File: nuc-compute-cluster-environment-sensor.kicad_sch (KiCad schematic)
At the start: 114 parts, among them J17 USB-C_GCT_USB4105-GF-A, J18 JST_SH_1x4_SM04B-SRSS-TB-LF-SN, U27 FT4232H_VQFN, U28 AP7370-33SA-7, U29 STM32G474CET6, U30 MB85RC1MTPNF-G, U31 SHT45, U32 BME280, Y2 Resonator_12MHz_ABM3B, Y3 Resonator_32.768kHz_ABS06, Y4 Resonator_8MHz_ABM3B

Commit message: 2nd part of review changes
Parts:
- added C104, C105: C_100n_0402, antmicro-footprints:C_0402_1005Metric, symbol antmicroCapacitors0402:C_100n_0402
- C68: DNP DNP -> (none)
- gave numbers to parts that had none: 2
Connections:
- net FTDI_+1V8: now also C104.1, C105.1
- net GND: now also C104.2, C105.2
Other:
- moved on the sheet: C92, TP60

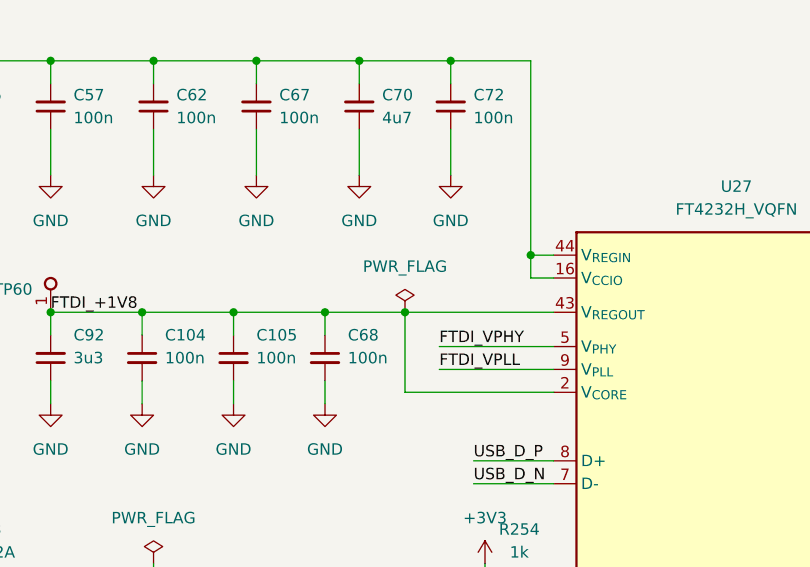
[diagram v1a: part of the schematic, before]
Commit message: Cleaning ERC on schematic
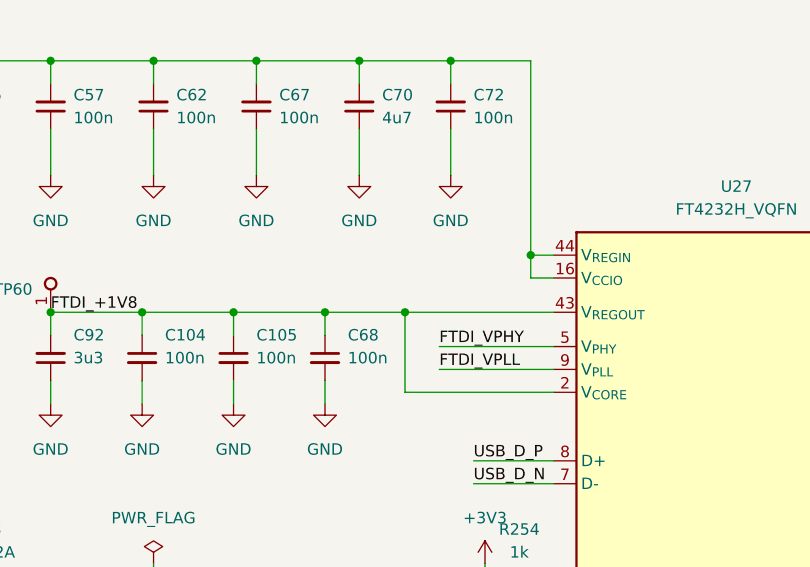
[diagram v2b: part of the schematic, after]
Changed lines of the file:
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@@
     (pin "2")
-  )
-  (symbol (lib_id "antmicropower:PWR_FLAG") (at 76.2 184.15 0) (unit 1)
-    (in_bom yes) (on_board yes) (fields_autoplaced)
-    (property "Reference" "#FLG07" (id 0) (at 76.2 182.245 0)
-      (effects (font (size 1.27 1.27)) hide)
-    )
-    (property "Value" "PWR_FLAG" (id 1) (at 76.2 179.07 0))
-    (property "Footprint" "" (id 2) (at 76.2 184.15 0)
-      (effects (font (size 1.27 1.27)) hide)
-    )
-    (property "Datasheet" "" (id 3) (at 76.2 184.15 0)
-      (effects (font (size 1.27 1.27)) hide)
-    )
-    (pin "1")
   )
   (symbol (lib_name "R_100k_0402_4") (lib_id "antmicroResistors0402:R_100k_0402") (at 307.34 139.7 90) (unit 1)

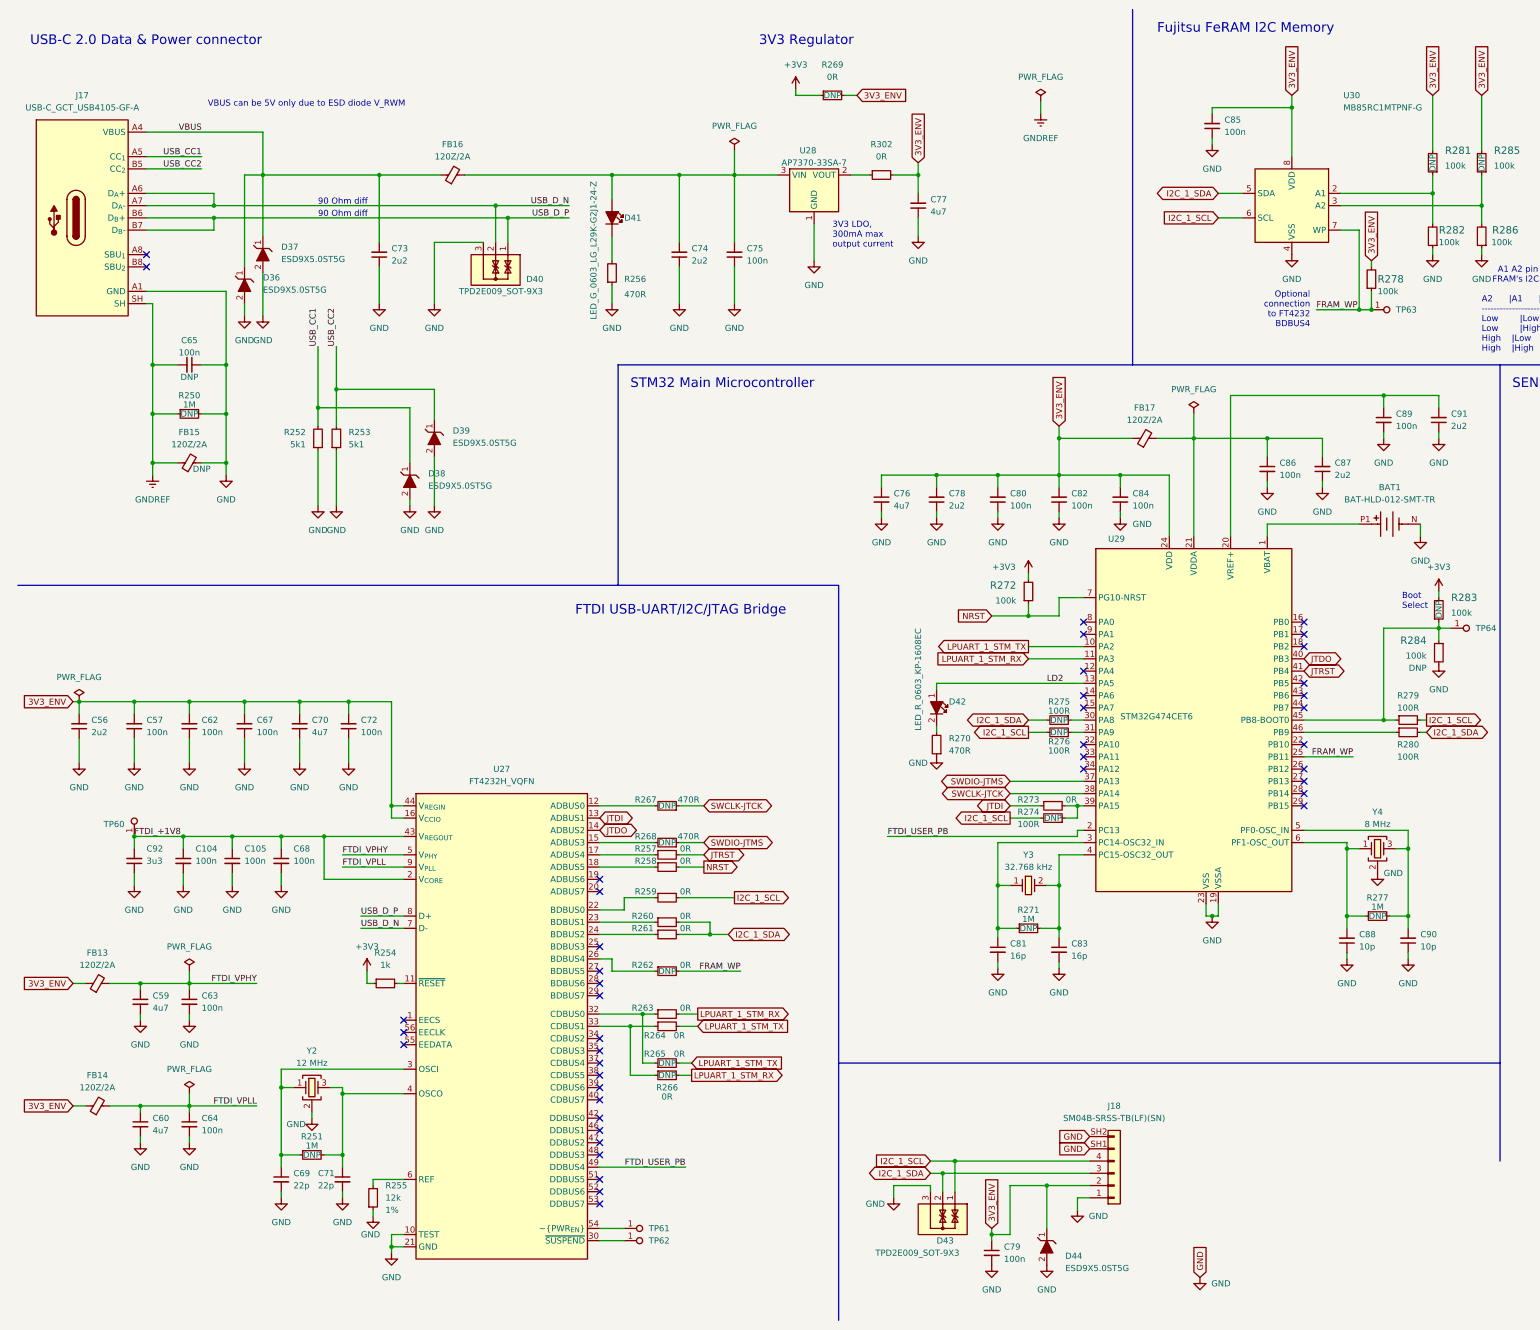
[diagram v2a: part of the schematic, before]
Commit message: Fix possible ERC errors
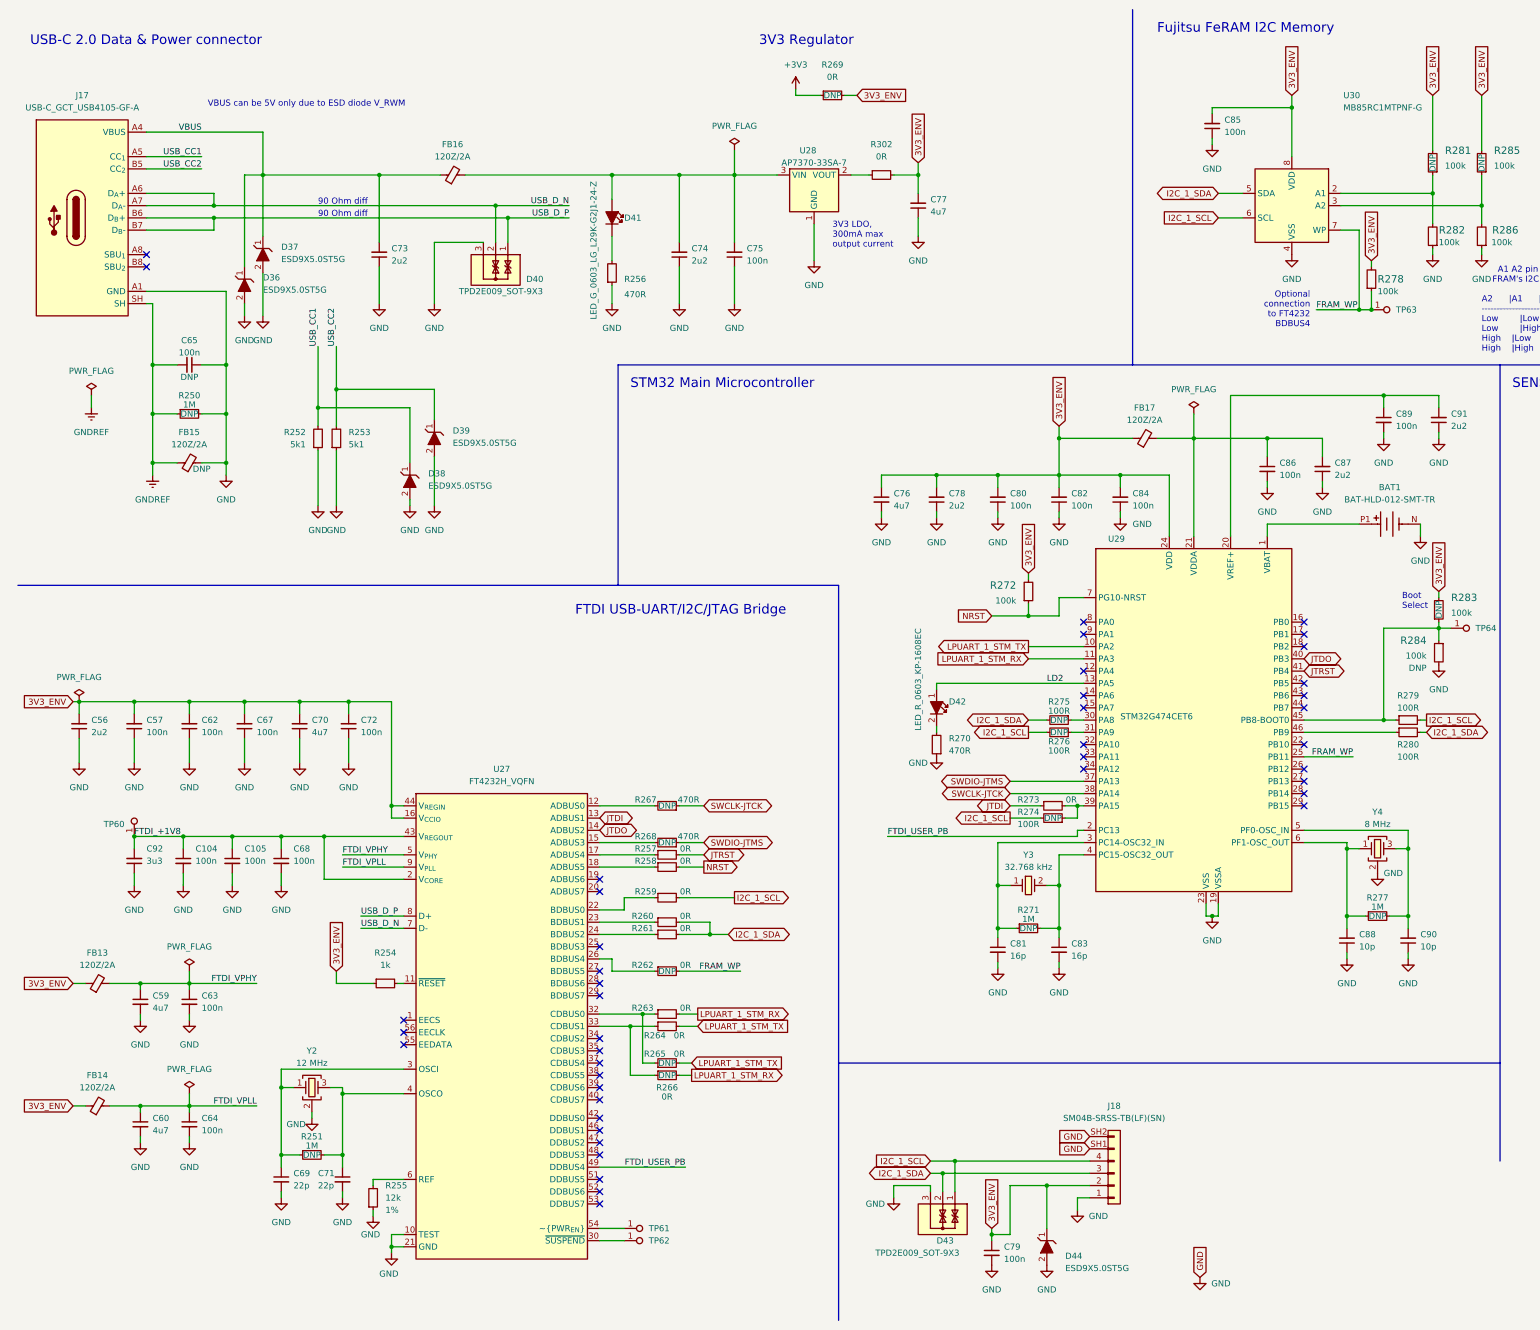
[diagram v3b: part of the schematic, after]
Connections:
- net +3V3: no longer R254.1, R272.2, R283.2
- net 3V3_ENV: now also R254.1, R272.2, R283.2

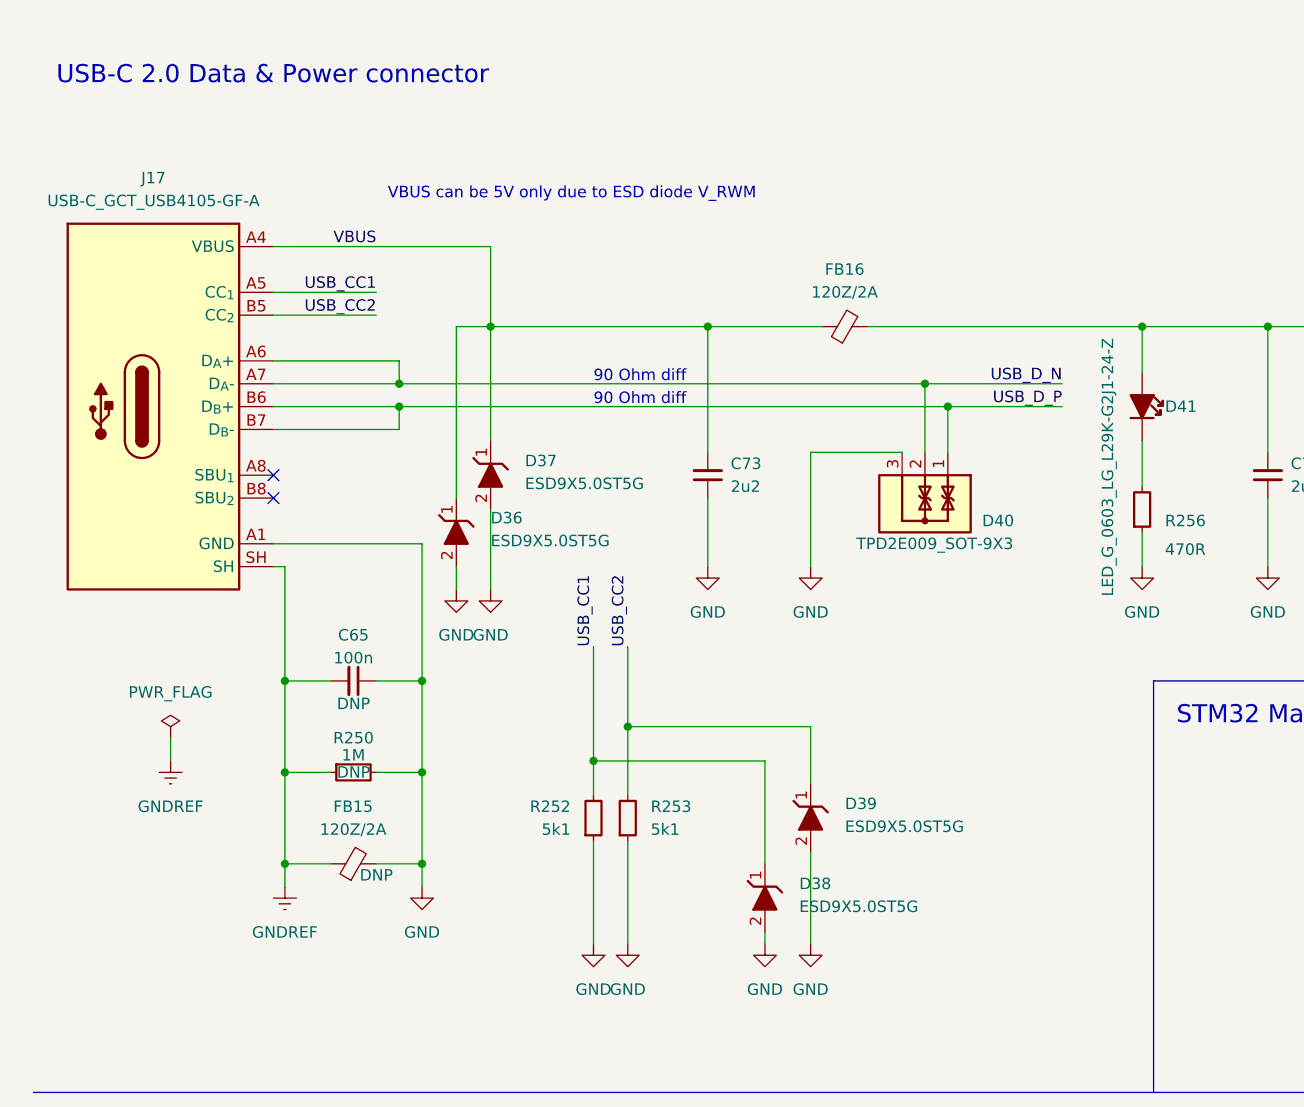
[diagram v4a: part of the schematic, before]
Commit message: Route fan signals for channel 1 and 2
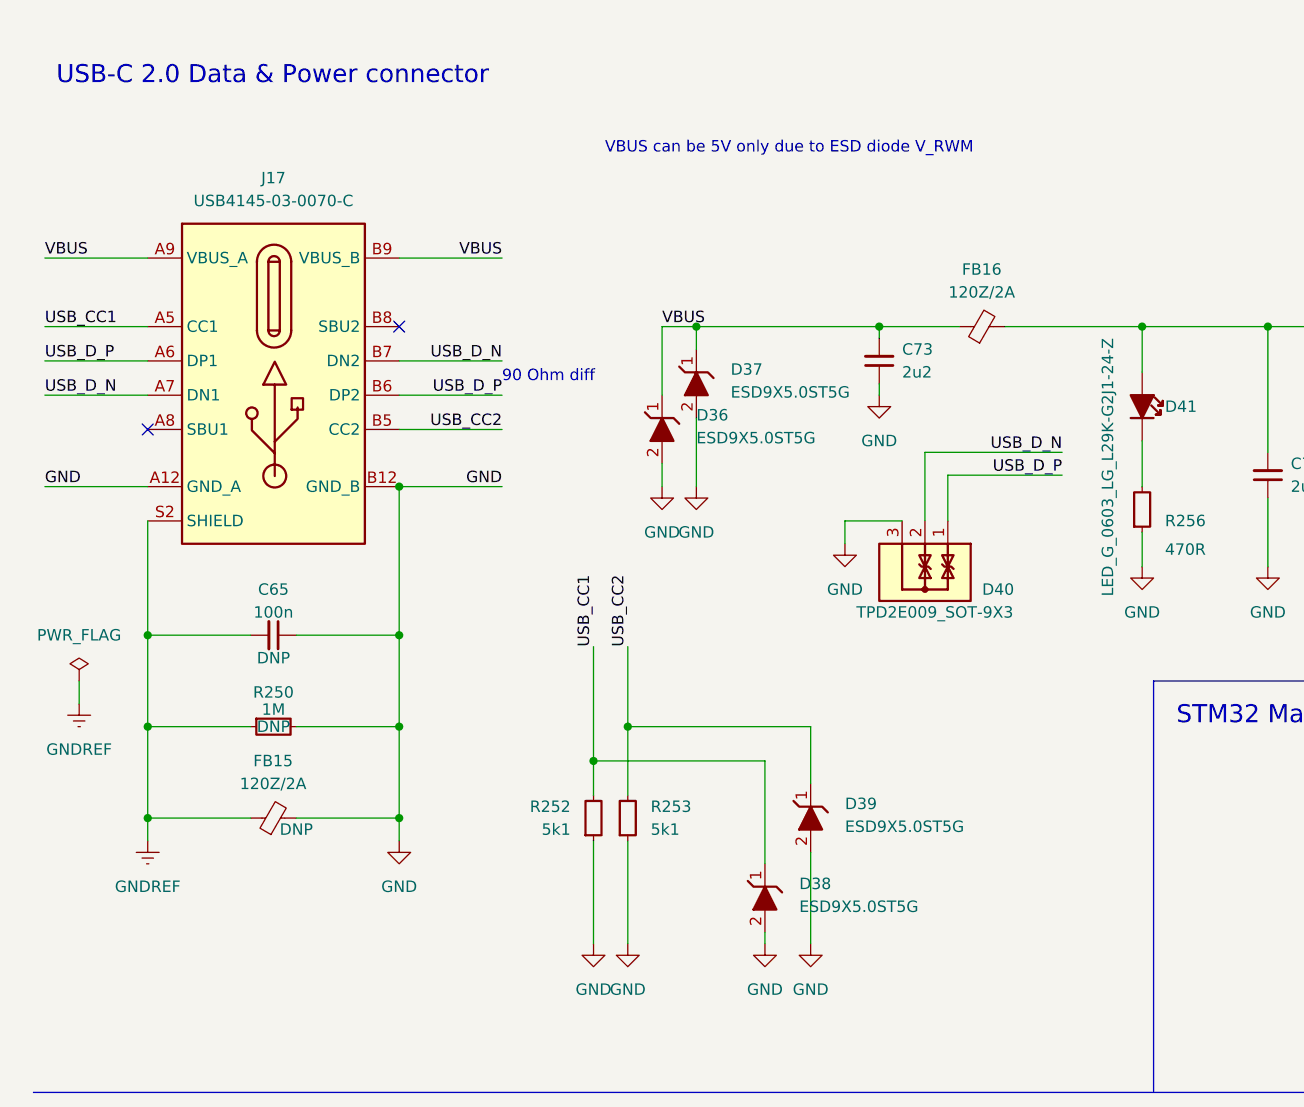
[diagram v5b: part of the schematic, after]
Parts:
- removed J17: USB-C_GCT_USB4105-GF-A, antmicro-footprints:USB-C_Receptacle_GCT_USB4105-GF-A, symbol antmicroUSBConnectors:USB-C_GCT_USB4105-GF-A
- added J17: USB-C_GCT_USB4145-03-0070-C, antmicro-footprints:USB-C_Receptacle_GCT_USB4145-03-0070-C, symbol antmicroUSBConnectors:USB-C_GCT_USB4145-03-0070-C
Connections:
- net GND: now also J17.A12 (GND_A), J17.B12 (GND_B)
- net GNDREF: now also J17.S2 (SHIELD)
- net USB_CC1: now also J17.A5 (CC1)
- net USB_CC2: now also J17.B5 (CC2)
- net USB_D_N: now also J17.A7 (DN1), J17.B7 (DN2)
- net USB_D_P: now also J17.A6 (DP1), J17.B6 (DP2)
- net VBUS: now also J17.A9 (VBUS_A), J17.B9 (VBUS_B)
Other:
- moved on the sheet: C65, C73, D36, D37, D40, FB15, FB16, R250

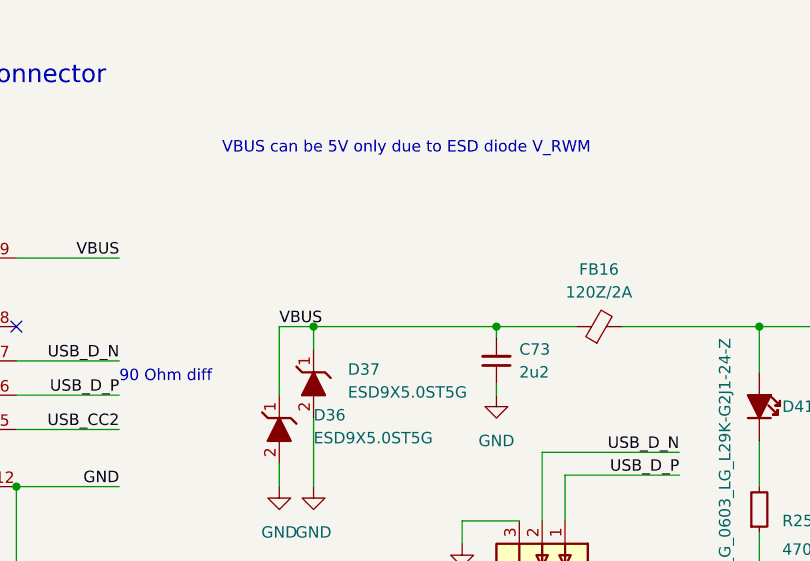
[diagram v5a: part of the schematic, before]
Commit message: Replace USB on schematic
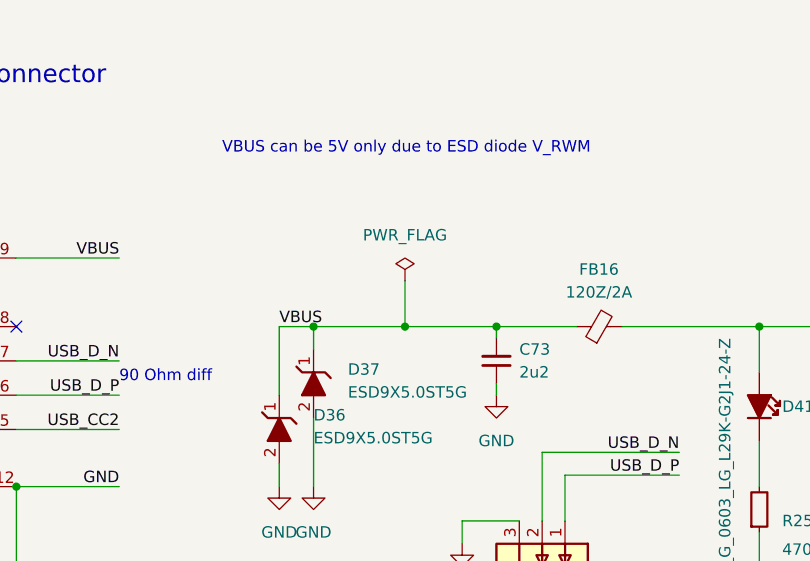
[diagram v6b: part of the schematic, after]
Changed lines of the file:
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@@
   (junction (at 293.37 74.93) (diameter 0) (color 0 0 0 0)
   )
+  (junction (at 96.52 46.99) (diameter 0) (color 0 0 0 0)
+  )
   (junction (at 90.17 177.8) (diameter 0) (color 0 0 0 0)
   )
@@
     (stroke (width 0) (type default) (color 0 0 0 0))
   )
-  (wire (pts (xy 86.36 46.99) (xy 106.68 46.99))
+  (wire (pts (xy 86.36 46.99) (xy 96.52 46.99))
     (stroke (width 0) (type default) (color 0 0 0 0))
   )
@@
     (stroke (width 0) (type default) (color 0 0 0 0))
   )
+  (wire (pts (xy 96.52 41.91) (xy 96.52 46.99))
+    (stroke (width 0) (type default) (color 0 0 0 0))
+  )
   (wire (pts (xy 271.78 105.41) (xy 271.78 101.6))
     (stroke (width 0) (type default) (color 0 0 0 0))
@@
     (stroke (width 0) (type default) (color 0 0 0 0))
   )
+  (wire (pts (xy 96.52 46.99) (xy 106.68 46.99))
+    (stroke (width 0) (type default) (color 0 0 0 0))
+  )
   (wire (pts (xy 279.4 167.64) (xy 289.56 167.64))
     (stroke (width 0) (type default) (color 0 0 0 0))
@@
     (pin "2")
   )
+  (symbol (lib_id "antmicropower:PWR_FLAG") (at 96.52 41.91 0) (unit 1)
+    (in_bom yes) (on_board yes) (fields_autoplaced)
+    (property "Reference" "#FLG0112" (id 0) (at 96.52 40.005 0)
+      (effects (font (size 1.27 1.27)) hide)
+    )
+    (property "Value" "PWR_FLAG" (id 1) (at 96.52 36.83 0))
+    (property "Footprint" "" (id 2) (at 96.52 41.91 0)
+      (effects (font (size 1.27 1.27)) hide)
+    )
+    (property "Datasheet" "" (id 3) (at 96.52 41.91 0)
+      (effects (font (size 1.27 1.27)) hide)
+    )
+    (pin "1")
+  )
   (symbol (lib_id "antmicroTVSDiodes:TPD2E009_SOT-9X3") (at 114.3 68.58 270) (unit 1)
